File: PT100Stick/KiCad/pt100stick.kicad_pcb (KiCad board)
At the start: 2 copper layers, 15.7 x 20.8 mm, 10 parts, among them U1 MAX31865ATP_

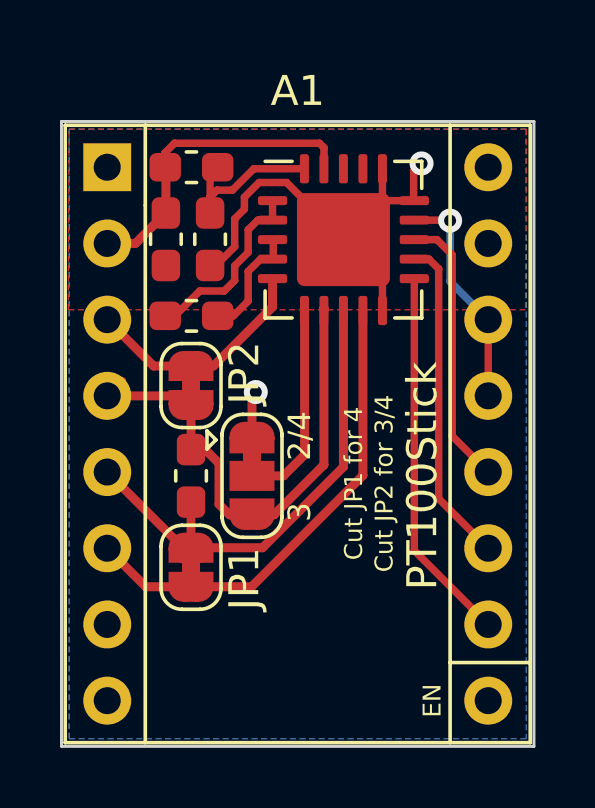
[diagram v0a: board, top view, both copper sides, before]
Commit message: move edgecuts
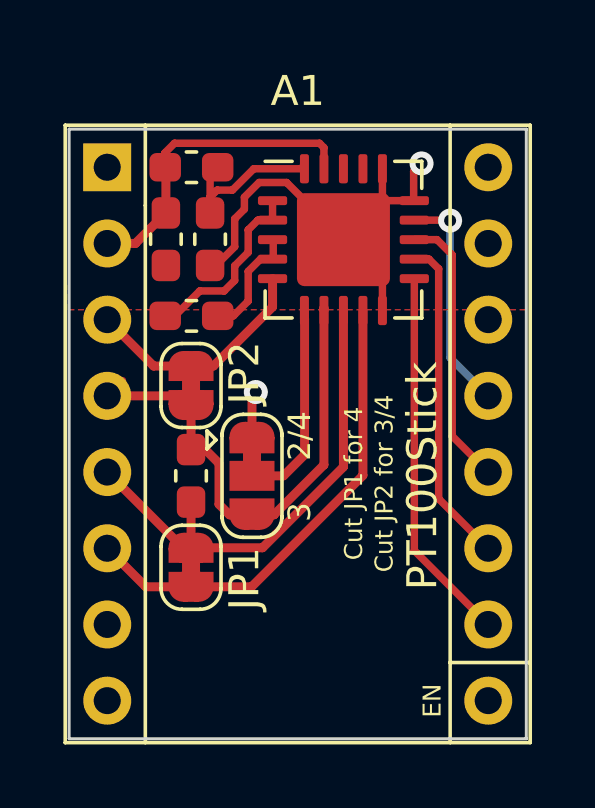
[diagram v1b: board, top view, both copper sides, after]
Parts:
- R1: value 430 -> 402
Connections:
- A1 pad 1: (no net) -> Net-(A1-Pad1)
- A1 pad 14: /MOSI -> Net-(A1-Pad14)
- A1 pad 15: (no net) -> Net-(A1-Pad15)
- A1 pad 16: (no net) -> Net-(A1-Pad16)
- A1 pad 8: (no net) -> +24V
- A1 pad 9: (no net) -> Net-(A1-Pad9)
- U1 pad 17: (no net) -> Net-(U1-Pad17)
- U1 pad 18: (no net) -> Net-(U1-Pad18)
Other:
- board size 15.7 x 20.8 mm -> 15.2 x 20.3 mm
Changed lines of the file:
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@@
-(kicad_pcb (version 20171130) (host pcbnew "(5.1.5)-3")
+(kicad_pcb (version 20171130) (host pcbnew "(5.1.4)-1")
   (general
     (thickness 1.6)
     (drawings 33)
-    (tracks 109)
+    (tracks 108)
     (zones 0)
     (modules 10)
-    (nets 15)
+    (nets 23)
   )
   (page A4)
@@
   (net 13 /FORCE2)
   (net 14 VDDA)
+  (net 15 "Net-(A1-Pad16)")
+  (net 16 "Net-(A1-Pad15)")
+  (net 17 "Net-(A1-Pad14)")
+  (net 18 "Net-(A1-Pad9)")
+  (net 19 "Net-(A1-Pad1)")
+  (net 20 "Net-(U1-Pad17)")
+  (net 21 "Net-(U1-Pad18)")
+  (net 22 +24V)
   (net_class Default "This is the default net class."
     (clearance 0.2)
@@
     (uvia_dia 0.3)
     (uvia_drill 0.1)
+    (add_net +24V)
     (add_net +3V3)
     (add_net /BIAS)
@@
     (add_net /SCK)
     (add_net GND)
+    (add_net "Net-(A1-Pad1)")
+    (add_net "Net-(A1-Pad14)")
+    (add_net "Net-(A1-Pad15)")
+    (add_net "Net-(A1-Pad16)")
+    (add_net "Net-(A1-Pad9)")
     (add_net "Net-(R1-Pad1)")
+    (add_net "Net-(U1-Pad17)")
+    (add_net "Net-(U1-Pad18)")
     (add_net VDDA)
   )
@@
       (effects (font (size 1 1) (thickness 0.15)))
     )
-    (pad 16 thru_hole oval (at 12.7 0) (size 1.6 1.6) (drill 0.9) (layers *.Cu *.Mask))
-    (pad 8 thru_hole oval (at 0 17.78) (size 1.6 1.6) (drill 0.9) (layers *.Cu *.Mask))
-    (pad 15 thru_hole oval (at 12.7 2.54) (size 1.6 1.6) (drill 0.9) (layers *.Cu *.Mask))
+    (pad 16 thru_hole oval (at 12.7 0) (size 1.6 1.6) (drill 0.9) (layers *.Cu *.Mask)
+      (net 15 "Net-(A1-Pad16)"))
+    (pad 8 thru_hole oval (at 0 17.78) (size 1.6 1.6) (drill 0.9) (layers *.Cu *.Mask)
+      (net 22 +24V))
+    (pad 15 thru_hole oval (at 12.7 2.54) (size 1.6 1.6) (drill 0.9) (layers *.Cu *.Mask)
+      (net 16 "Net-(A1-Pad15)"))
     (pad 7 thru_hole oval (at 0 15.24) (size 1.6 1.6) (drill 0.9) (layers *.Cu *.Mask)
       (net 1 GND))
     (pad 14 thru_hole oval (at 12.7 5.08) (size 1.6 1.6) (drill 0.9) (layers *.Cu *.Mask)
-      (net 5 /MOSI))
+      (net 17 "Net-(A1-Pad14)"))
     (pad 6 thru_hole oval (at 0 12.7) (size 1.6 1.6) (drill 0.9) (layers *.Cu *.Mask)
       (net 10 /FORCE-))
@@
     (pad 2 thru_hole oval (at 0 2.54) (size 1.6 1.6) (drill 0.9) (layers *.Cu *.Mask)
       (net 6 +3V3))
-    (pad 9 thru_hole oval (at 12.7 17.78) (size 1.6 1.6) (drill 0.9) (layers *.Cu *.Mask))
-    (pad 1 thru_hole rect (at 0 0) (size 1.6 1.6) (drill 0.9) (layers *.Cu *.Mask))
+    (pad 9 thru_hole oval (at 12.7 17.78) (size 1.6 1.6) (drill 0.9) (layers *.Cu *.Mask)
+      (net 18 "Net-(A1-Pad9)"))
+    (pad 1 thru_hole rect (at 0 0) (size 1.6 1.6) (drill 0.9) (layers *.Cu *.Mask)
+      (net 19 "Net-(A1-Pad1)"))
     (model ${KISYS3DMOD}/Module.3dshapes/Pololu_Breakout-16_15.2x20.3mm.wrl
       (at (xyz 0 0 0))
@@
       (effects (font (size 1 1) (thickness 0.15)))
     )
-    (fp_text value 430 (at 0 1.43) (layer F.Fab)
+    (fp_text value 402 (at 0 1.43) (layer F.Fab)
       (effects (font (size 1 1) (thickness 0.15)))
     )
@@
     (pad 16 smd roundrect (at 1.3 -2.3625) (size 0.3 0.975) (layers F.Cu F.Paste F.Mask) (roundrect_rratio 0.25)
       (net 1 GND))
-    (pad 17 smd roundrect (at 0.65 -2.3625) (size 0.3 0.975) (layers F.Cu F.Paste F.Mask) (roundrect_rratio 0.25))
-    (pad 18 smd roundrect (at 0 -2.3625) (size 0.3 0.975) (layers F.Cu F.Paste F.Mask) (roundrect_rratio 0.25))
+    (pad 17 smd roundrect (at 0.65 -2.3625) (size 0.3 0.975) (layers F.Cu F.Paste F.Mask) (roundrect_rratio 0.25)
+      (net 20 "Net-(U1-Pad17)"))
+    (pad 18 smd roundrect (at 0 -2.3625) (size 0.3 0.975) (layers F.Cu F.Paste F.Mask) (roundrect_rratio 0.25)
+      (net 21 "Net-(U1-Pad18)"))
     (pad 19 smd roundrect (at -0.65 -2.3625) (size 0.3 0.975) (layers F.Cu F.Paste F.Mask) (roundrect_rratio 0.25)
       (net 6 +3V3))
@@
     (effects (font (size 0.75 0.75) (thickness 0.15)))
   )
-  (gr_line (start 156.464 69.596) (end 156.464 90.424) (layer Edge.Cuts) (width 0.1))
-  (gr_line (start 140.716 69.596) (end 156.464 69.596) (layer Edge.Cuts) (width 0.1))
-  (gr_line (start 140.716 90.424) (end 140.716 69.596) (layer Edge.Cuts) (width 0.1))
-  (gr_line (start 156.464 90.424) (end 140.716 90.424) (layer Edge.Cuts) (width 0.1))
+  (gr_line (start 156.21 69.85) (end 156.21 90.17) (layer Edge.Cuts) (width 0.1))
+  (gr_line (start 140.97 69.85) (end 156.21 69.85) (layer Edge.Cuts) (width 0.1))
+  (gr_line (start 140.97 90.17) (end 140.97 69.85) (layer Edge.Cuts) (width 0.1))
+  (gr_line (start 156.21 90.17) (end 140.97 90.17) (layer Edge.Cuts) (width 0.1))
   (segment (start 151.414 71.193) (end 151.414 72.233) (width 0.25) (layer F.Cu) (net 1) (status 30))
   (segment (start 151.414 72.233) (end 150.114 73.533) (width 0.25) (layer F.Cu) (net 1) (status 30))
@@
   (segment (start 153.28901 82.16901) (end 154.94 83.82) (width 0.25) (layer F.Cu) (net 4) (status 20))
   (segment (start 152.964 74.183) (end 153.28901 74.50801) (width 0.25) (layer F.Cu) (net 4))
-  (segment (start 154.94 78.74) (end 154.94 76.2) (width 0.25) (layer F.Cu) (net 5) (status 30))
   (segment (start 154.559 78.359) (end 154.94 78.74) (width 0.25) (layer B.Cu) (net 5) (status 30))
   (segment (start 154.686 78.994) (end 154.94 78.74) (width 0.25) (layer B.Cu) (net 5) (status 30))
@@
   (segment (start 152.4765 72.883) (end 153.655 72.883) (width 0.25) (layer F.Cu) (net 5) (status 10))
   (segment (start 153.655 72.883) (end 153.67 72.898) (width 0.25) (layer F.Cu) (net 5))
-  (segment (start 153.67 74.93) (end 154.94 76.2) (width 0.25) (layer B.Cu) (net 5) (status 20))
-  (segment (start 153.67 72.898) (end 153.67 74.93) (width 0.25) (layer B.Cu) (net 5))
+  (segment (start 153.67 77.47) (end 153.67 72.898) (width 0.25) (layer B.Cu) (net 5))
+  (segment (start 154.94 78.74) (end 153.67 77.47) (width 0.25) (layer B.Cu) (net 5))
   (segment (start 144.48401 70.31999) (end 149.31599 70.31999) (width 0.25) (layer F.Cu) (net 6))
   (segment (start 149.31599 70.31999) (end 149.464 70.468) (width 0.25) (layer F.Cu) (net 6))
